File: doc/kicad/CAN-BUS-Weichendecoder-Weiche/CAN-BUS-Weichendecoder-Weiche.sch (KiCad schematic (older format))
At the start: 39 parts, among them J1 250-1404, J1001 I²C, J1002 Conn_01x16_Male, J2 250-1404, J3 250-1404, J31 12V DC, J4 250-1404, J41 2604-1102, J5 250-1404, U1 Arduino_Nano, U10 TSR_1-2450, U1001 6N136, U2 ULN2803A, U3 ULN2803A

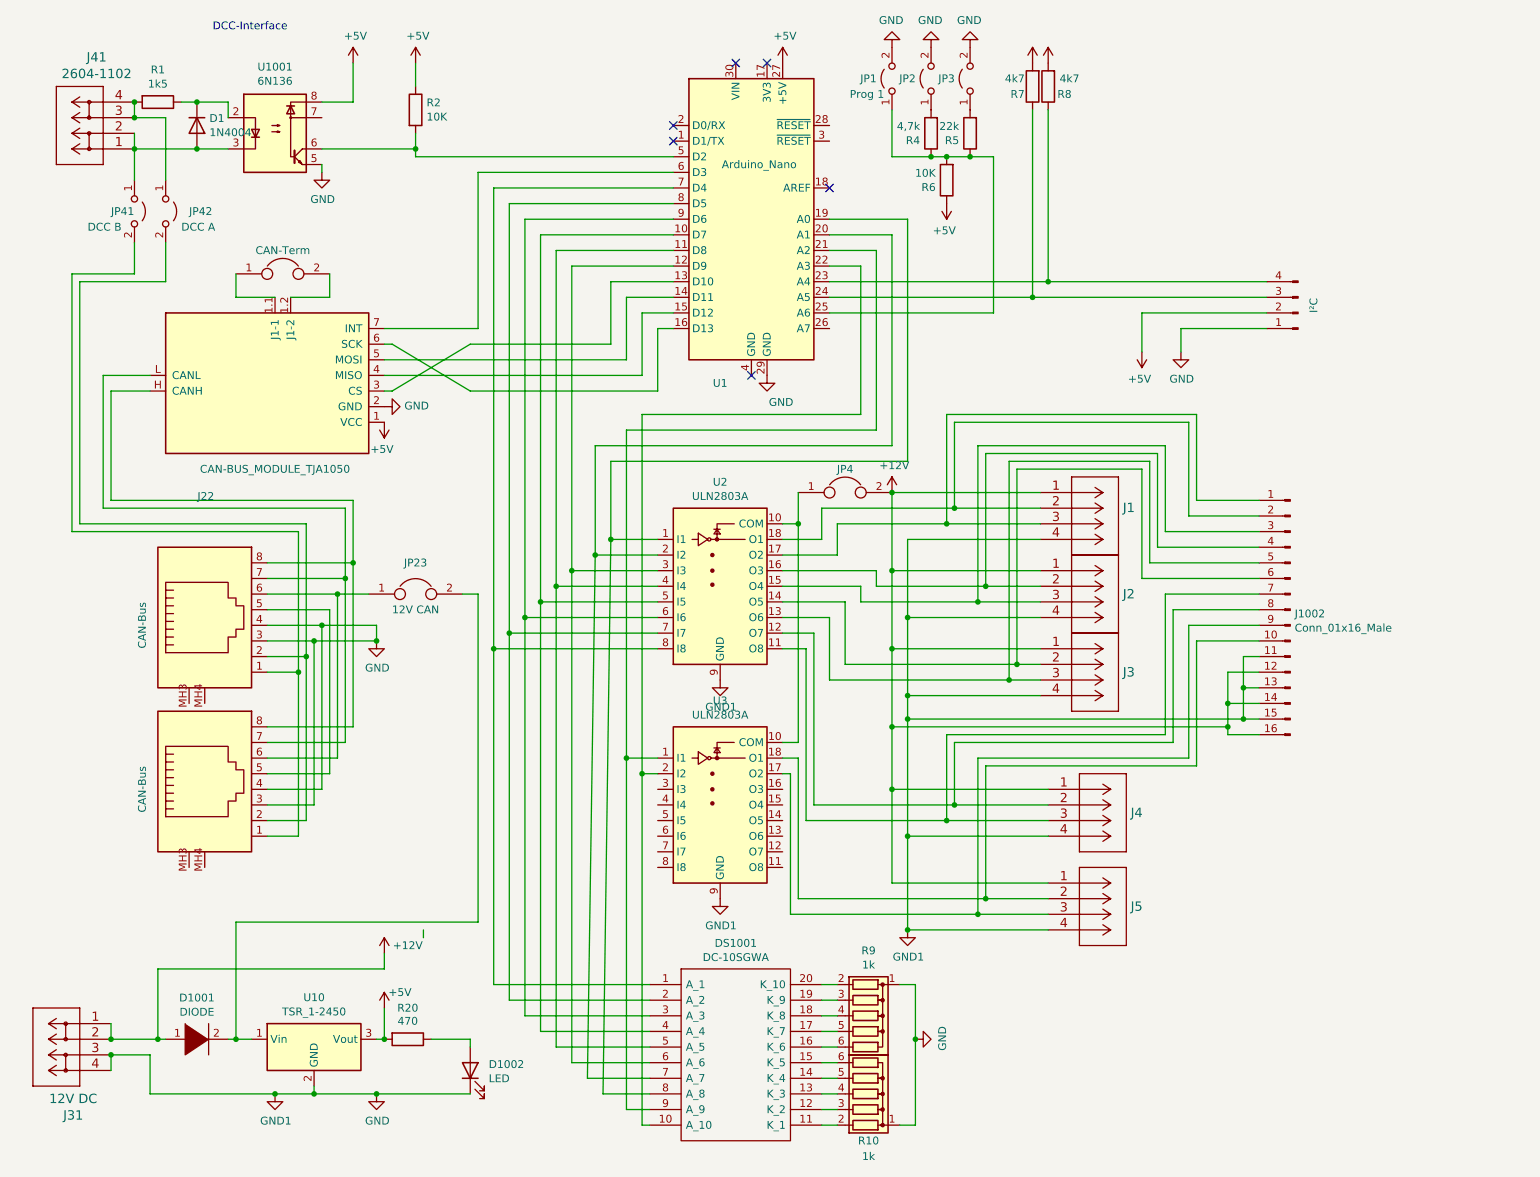
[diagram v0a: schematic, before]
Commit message: Buchen und Stecker vertauscht und Anordnung kompakter
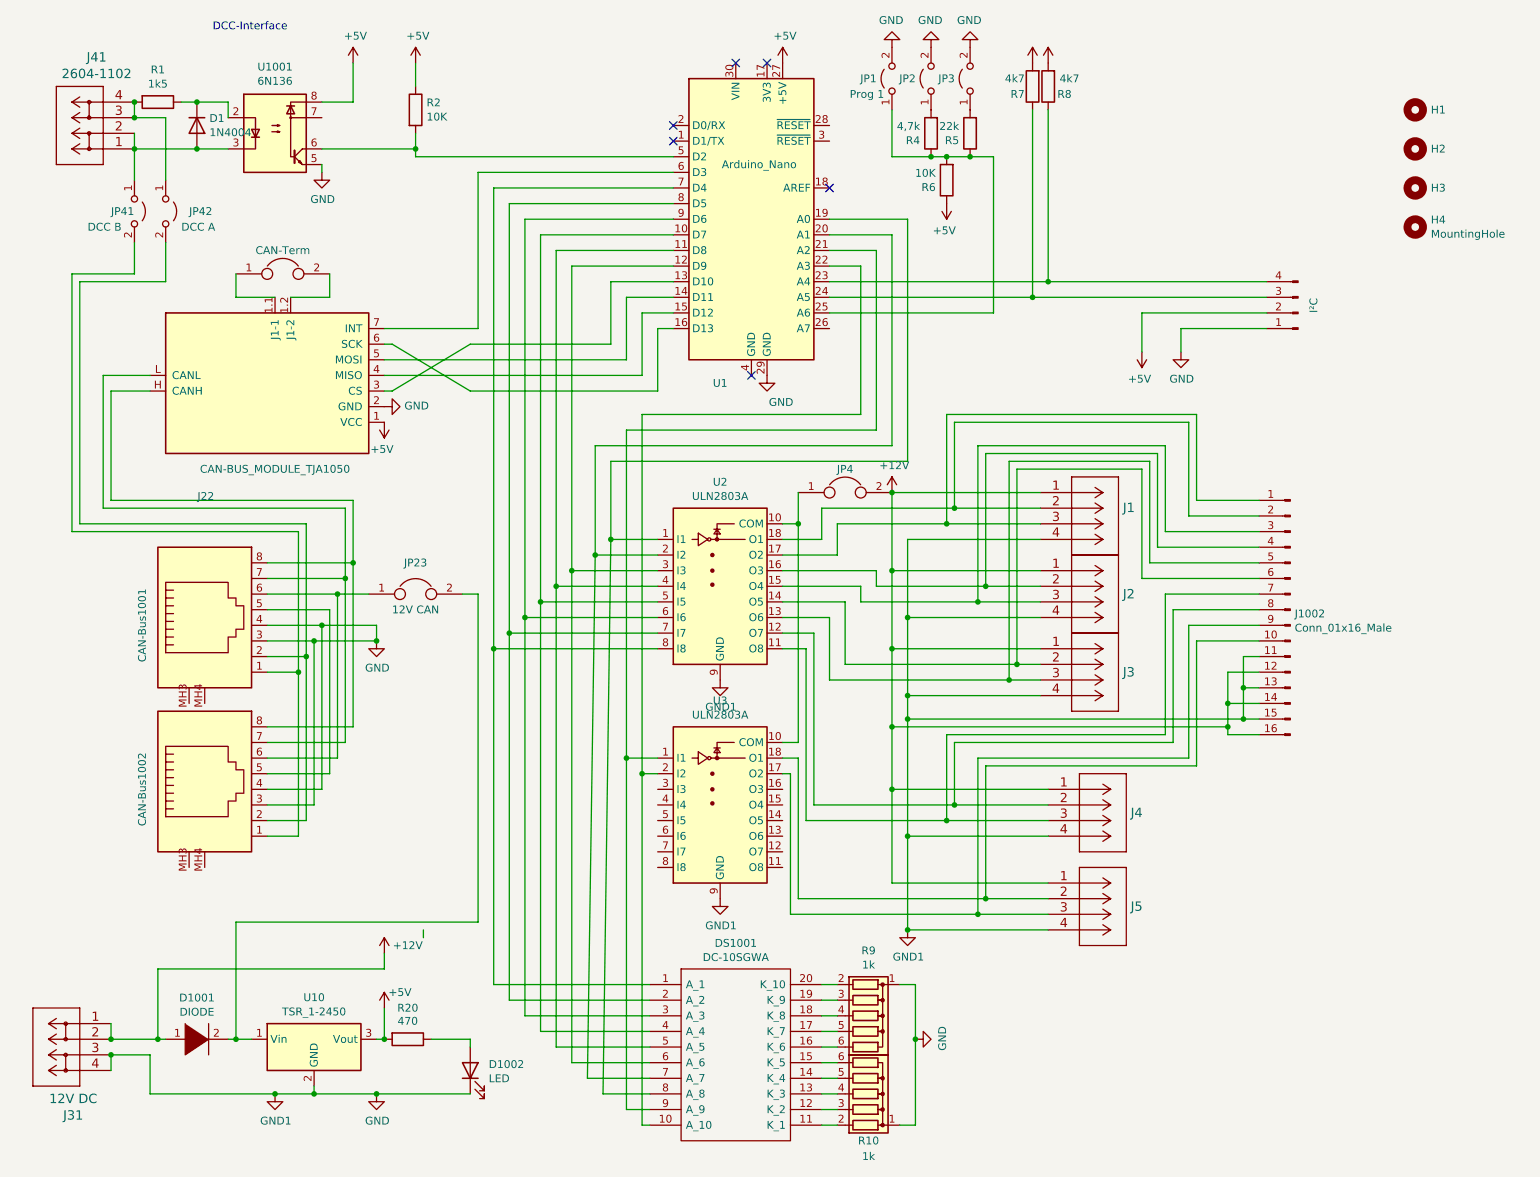
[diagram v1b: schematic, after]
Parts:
- added H1, H2, H3, H4: MountingHole, Mounting_Holes:MountingHole_3.2mm_M3, symbol Mechanical:MountingHole
- renumbered CAN-Bus to CAN-Bus1001, CAN-Bus to CAN-Bus1002
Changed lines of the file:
@@
 	2950 2850 2900 2850
 $Comp
-L ASSMANN_WSW:A-20042-LP_FS CAN-Bus
+L ASSMANN_WSW:A-20042-LP_FS CAN-Bus1002
 U 1 1 60B7A5DF
 P 1700 5150
-F 0 "CAN-Bus" V 1350 4900 50  0000 C CNN
+F 0 "CAN-Bus1002" V 1350 4900 50  0000 C CNN
 F 1 "J22" H 1757 5726 50  0001 C CNN
 F 2 "ASSMANN_WSW:A20042LPFS" V 1700 5175 50  0001 C CNN
@@
 Connection ~ 4550 5300
 $Comp
-L ASSMANN_WSW:A-20042-LP_FS CAN-Bus
+L ASSMANN_WSW:A-20042-LP_FS CAN-Bus1001
 U 1 1 64B4E74A
 P 1700 4100
-F 0 "CAN-Bus" V 1350 3850 50  0000 C CNN
+F 0 "CAN-Bus1001" V 1350 3850 50  0000 C CNN
 F 1 "J22" H 1757 4676 50  0000 C CNN
 F 2 "ASSMANN_WSW:A20042LPFS" V 1700 4125 50  0001 C CNN
@@
 Wire Wire Line
 	5550 3700 5550 3500
+$Comp
+L Mechanical:MountingHole H1
+U 1 1 617C993C
+P 9500 1050
+F 0 "H1" H 9600 1050 50  0000 L CNN
+F 1 "MountingHole" H 9600 1005 50  0001 L CNN
+F 2 "Mounting_Holes:MountingHole_3.2mm_M3" H 9500 1050 50  0001 C CNN
+F 3 "~" H 9500 1050 50  0001 C CNN
+	1    9500 1050
+	1    0    0    -1
+$EndComp
+$Comp
+L Mechanical:MountingHole H2
+U 1 1 617E4E10
+P 9500 1300
+F 0 "H2" H 9600 1300 50  0000 L CNN
+F 1 "MountingHole" H 9600 1255 50  0001 L CNN
+F 2 "Mounting_Holes:MountingHole_3.2mm_M3" H 9500 1300 50  0001 C CNN
+F 3 "~" H 9500 1300 50  0001 C CNN
+	1    9500 1300
+	1    0    0    -1
+$EndComp
+$Comp
+L Mechanical:MountingHole H3
+U 1 1 617FE630
+P 9500 1550
+F 0 "H3" H 9600 1550 50  0000 L CNN
+F 1 "MountingHole" H 9600 1505 50  0001 L CNN
+F 2 "Mounting_Holes:MountingHole_3.2mm_M3" H 9500 1550 50  0001 C CNN
+F 3 "~" H 9500 1550 50  0001 C CNN
+	1    9500 1550
+	1    0    0    -1
+$EndComp
+$Comp
+L Mechanical:MountingHole H4
+U 1 1 61831DA5
+P 9500 1800
+F 0 "H4" H 9600 1846 50  0000 L CNN
+F 1 "MountingHole" H 9600 1755 50  0000 L CNN
+F 2 "Mounting_Holes:MountingHole_3.2mm_M3" H 9500 1800 50  0001 C CNN
+F 3 "~" H 9500 1800 50  0001 C CNN
+	1    9500 1800
+	1    0    0    -1
+$EndComp
 $EndSCHEMATC

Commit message: Anordnung der Bauteile kompakter, 2 statt 3 prog-Pins, nur eine Verbindung zur Weiche
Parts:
- removed J1002: Conn_01x16_Male, Connectors:he10-16d, symbol Connector:Conn_01x16_Male
- removed JP1: Prog 1, Pin_Headers:Pin_Header_Straight_1x02_Pitch2.54mm, symbol Jumper:Jumper_2_Open
- added D3: 1N4001, Diodes_THT:D_DO-41_SOD81_P7.62mm_Horizontal, symbol Device:D
- D2: renamed from D1001; value DIODE -> 1N4001; footprint Diodes_THT:D_DO-15_P10.16mm_Horizontal -> Diodes_THT:D_DO-41_SOD81_P7.62mm_Horizontal; symbol pspice:DIODE -> Device:D
- J1, J2, J3, J4, J5: footprint Wago:250-1404 -> Wago:CONN_250-1404_WAG
- J22: renamed from CAN-Bus1001; value J22 -> CAN-BUS
- J23: renamed from CAN-Bus1002; value J22 -> CAN-BUS
- J6: renamed from J31; value 12V DC -> GND 12V DC +
- J7: renamed from J41; value 2604-1102 -> DCC IN
- J8: renamed from J1001; value I²C -> I²C D C + -
- JP2: renamed from JP42; value DCC A -> DCC CAN
- JP5: renamed from JP2; value Prog2 -> Prog1
- JP6: renamed from JP3; value Prog3 -> Prog2
- JP7: renamed from JP4; value Jumper -> COM
- Shield1: renamed from Shield1001; value CAN-BUS_MODULE_TJA1050 -> CAN-BUS-MODULE; footprint CAN-BUS-MODULE:MCP2515_CAN_MODULE_BY0-10 -> CAN-BUS-MODULE:MCP2515_CAN_MODULE
- renumbered D1002 to D4, DS1001 to DS1, JP41 to JP1, JP11 to JP3, JP23 to JP4, U1001 to U1, U1 to U2, U2 to U3, U3 to U4, U10 to U5
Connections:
- net +12V: now also D2.2 (A), J1.2, J2.2, J3.2, J4.2, J5.2; no longer D2.1 (K), J1.1, J2.1, J3.1, J4.1, J5.1
- net at DS1.9 (A_9), U2.21 (A2): now also U4.3 (I3); no longer U4.1 (I1)
- net at DS1.10 (A_10), U2.22 (A3): now also U4.4 (I4); no longer U4.2 (I2)
- net at DS1.1 (A_1), U2.7 (D4): now also U4.2 (I2); no longer U3.8 (I8)
- net at DS1.2 (A_2), U2.8 (D5): now also U4.1 (I1); no longer U3.7 (I7)
- net at U3.11 (O8): no longer J4.3
- net at U3.12 (O7): no longer J4.2
- net at U3.14 (O5): now also J3.1; no longer J3.2
- net at U3.16 (O3): now also J2.1; no longer J2.2
- net at U3.18 (O1): now also J1.1; no longer J1.2
- net at U4.15 (O4): now also J5.3
- net at U4.16 (O3): now also J5.1
- net at U4.17 (O2): now also J4.3; no longer J5.3
- net at U4.18 (O1): now also J4.1; no longer J5.2
- new net: D2.1 (K), D3.1 (K), U5.1 (Vin)
- new net: D3.2 (A), JP4.2
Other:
- note added: "B A"
- moved on the sheet: JP5, JP7, R4

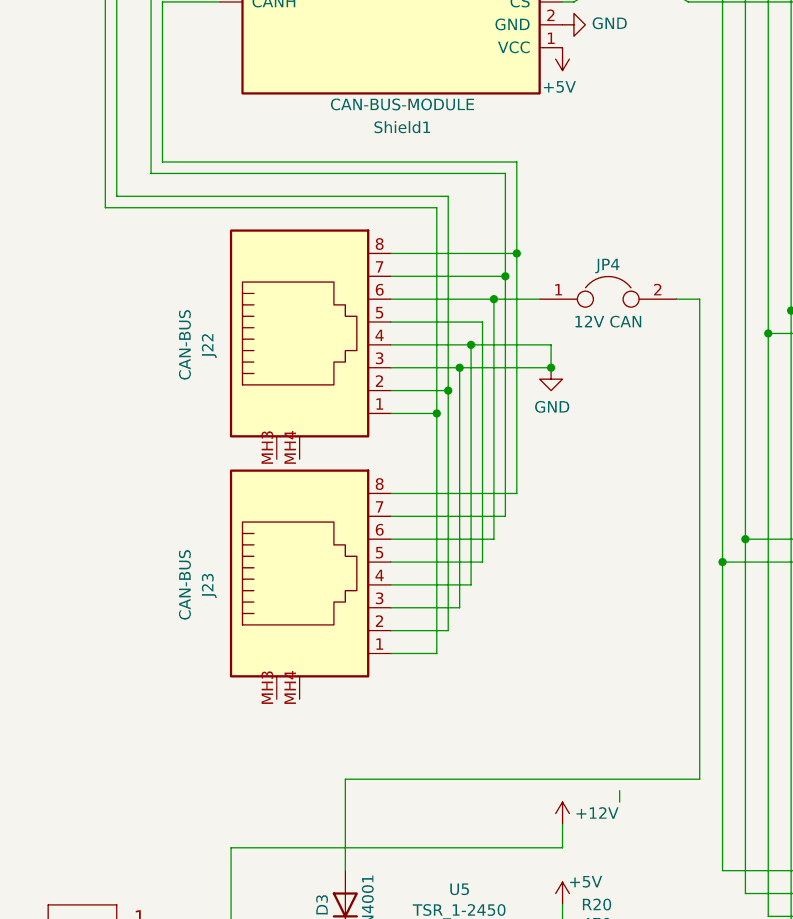
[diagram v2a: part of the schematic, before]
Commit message: CAN-Bus-Belegun geändert
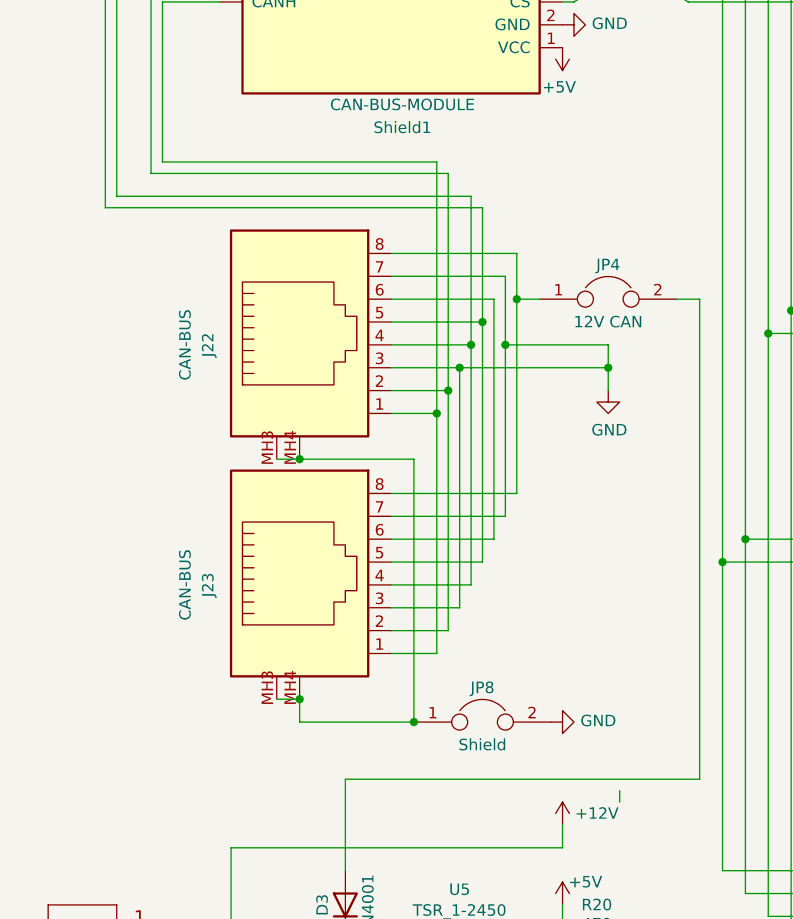
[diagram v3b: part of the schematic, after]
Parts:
- added JP8: Shield, Pin_Headers:Pin_Header_Straight_1x02_Pitch2.54mm, symbol Device:Jumper
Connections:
- net GND: now also J22.7, J23.7, JP8.2; no longer J22.4, J23.4
- net at J22.8, J23.8: now also JP4.1; no longer Shield1.H (CANH)
- net at J22.1, J23.1: now also Shield1.H (CANH); no longer JP1.2 (B)
- net at J22.2, J23.2: now also Shield1.L (CANL); no longer JP2.2 (B)
- net at J22.5, J23.5: now also JP1.2 (B)
- net at J22.6, J23.6: no longer JP4.1
- net at J23.MH3: now also J22.MH3, J22.MH4, J23.MH4, JP8.1
- new net: J22.4, J23.4, JP2.2 (B)
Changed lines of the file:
@@
 	2600 5200 2150 5200
 Wire Wire Line
-	2650 4050 2650 5100
+	2650 4050 2650 4350
 Wire Wire Line
 	2650 5100 2150 5100
 Wire Wire Line
-	2700 3950 2700 5000
+	2700 3950 2700 4150
 Wire Wire Line
 	2700 5000 2150 5000
@@
 	2450 4450 2450 5500
 Wire Wire Line
-	1100 3600 2650 3600
-Connection ~ 2650 4050
+	1100 3600 2400 3600
 Wire Wire Line
 	2150 3950 2700 3950
 Wire Wire Line
-	1150 3550 2700 3550
-Connection ~ 2700 3950
-Wire Wire Line
-	2850 4350 2500 4350
-Connection ~ 2500 4350
-Wire Wire Line
-	2850 4450 2450 4450
-Connection ~ 2450 4450
-$Comp
-L power:GND #PWR0101
-U 1 1 64C41938
-P 2850 4450
-F 0 "#PWR0101" H 2850 4200 50  0001 C CNN
-F 1 "GND" H 2855 4277 50  0000 C CNN
-F 2 "" H 2850 4450 50  0001 C CNN
-F 3 "" H 2850 4450 50  0001 C CNN
-	1    2850 4450
-	1    0    0    -1
-$EndComp
-Wire Wire Line
-	2850 4350 2850 4450
-Connection ~ 2850 4450
+	1150 3550 2350 3550
 $Comp
 L Jumper:Jumper_2_Open JP1
@@
 	1500 1100 1500 1500
 Wire Wire Line
-	2400 4550 2400 3700
-Wire Wire Line
-	2400 3700 950  3700
-Wire Wire Line
 	950  3700 950  2150
 Wire Wire Line
@@
 Wire Wire Line
 	1500 2150 1500 1900
-Connection ~ 2400 4550
-Wire Wire Line
-	2350 4650 2350 3750
-Wire Wire Line
-	2350 3750 900  3750
 Wire Wire Line
 	900  3750 900  2100
@@
 Wire Wire Line
 	1300 2100 1300 1900
-Connection ~ 2350 4650
 $Comp
 L Device:Jumper JP4
@@
 	1    0    0    -1
 $EndComp
-Wire Wire Line
-	2600 4150 2800 4150
-Connection ~ 2600 4150
-Wire Wire Line
-	2650 3600 2650 4050
-Wire Wire Line
-	2700 3550 2700 3950
 $Comp
 L power:+5V #PWR01044
@@
 Text Notes 800  1150 1    50   ~ 0
 B  A
+Wire Wire Line
+	1650 5900 1750 5900
+Wire Wire Line
+	2250 4850 2250 6000
+Wire Wire Line
+	2250 6000 1750 6000
+Wire Wire Line
+	1750 6000 1750 5900
+Wire Wire Line
+	1650 4850 1750 4850
+Connection ~ 1750 4850
+Wire Wire Line
+	1750 4850 2250 4850
+Connection ~ 1750 5900
+$Comp
+L Device:Jumper JP8
+U 1 1 618B66A0
+P 2550 6000
+F 0 "JP8" H 2550 6150 50  0000 C CNN
+F 1 "Shield" H 2550 5900 50  0000 C CNN
+F 2 "Pin_Headers:Pin_Header_Straight_1x02_Pitch2.54mm" H 2550 6000 50  0001 C CNN
+F 3 "~" H 2550 6000 50  0001 C CNN
+	1    2550 6000
+	1    0    0    -1
+$EndComp
+Connection ~ 2250 6000
+$Comp
+L power:GND #PWR0101
+U 1 1 618B7783
+P 2850 6000
+F 0 "#PWR0101" H 2850 5750 50  0001 C CNN
+F 1 "GND" V 2855 5872 50  0000 R CNN
+F 2 "" H 2850 6000 50  0001 C CNN
+F 3 "" H 2850 6000 50  0001 C CNN
+	1    2850 6000
+	0    -1   -1   0
+$EndComp
+Wire Wire Line
+	2350 4650 2350 3550
+Connection ~ 2350 4650
+Wire Wire Line
+	2400 4550 2400 3600
+Connection ~ 2400 4550
+$Comp
+L power:GND #PWR0108
+U 1 1 6197F624
+P 3100 4550
+F 0 "#PWR0108" H 3100 4300 50  0001 C CNN
+F 1 "GND" H 3105 4377 50  0000 C CNN
+F 2 "" H 3100 4550 50  0001 C CNN
+F 3 "" H 3100 4550 50  0001 C CNN
+	1    3100 4550
+	1    0    0    -1
+$EndComp
+Wire Wire Line
+	2450 4450 3100 4450
+Wire Wire Line
+	3100 4450 3100 4550
+Connection ~ 2450 4450
+Wire Wire Line
+	2650 4350 3100 4350
+Wire Wire Line
+	3100 4350 3100 4450
+Connection ~ 2650 4350
+Wire Wire Line
+	2650 4350 2650 5100
+Connection ~ 3100 4450
+Wire Wire Line
+	2700 4150 2800 4150
+Connection ~ 2700 4150
+Wire Wire Line
+	2700 4150 2700 5000
+Wire Wire Line
+	2500 4350 2500 3700
+Connection ~ 2500 4350
+Wire Wire Line
+	2500 3700 950  3700
+Wire Wire Line
+	2550 4250 2550 3750
+Connection ~ 2550 4250
+Wire Wire Line
+	2550 3750 900  3750
 $EndSCHEMATC
